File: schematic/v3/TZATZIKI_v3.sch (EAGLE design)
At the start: 7 parts, among them J1 2X20-CHIP-HEADERS2X20CHIP_OFF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, J2 USD-SDIO-SOCKET, J3 USD-SDIO-SOCKET, J4 USD-SDIO-SOCKET, J5 USD-SDIO-SOCKET

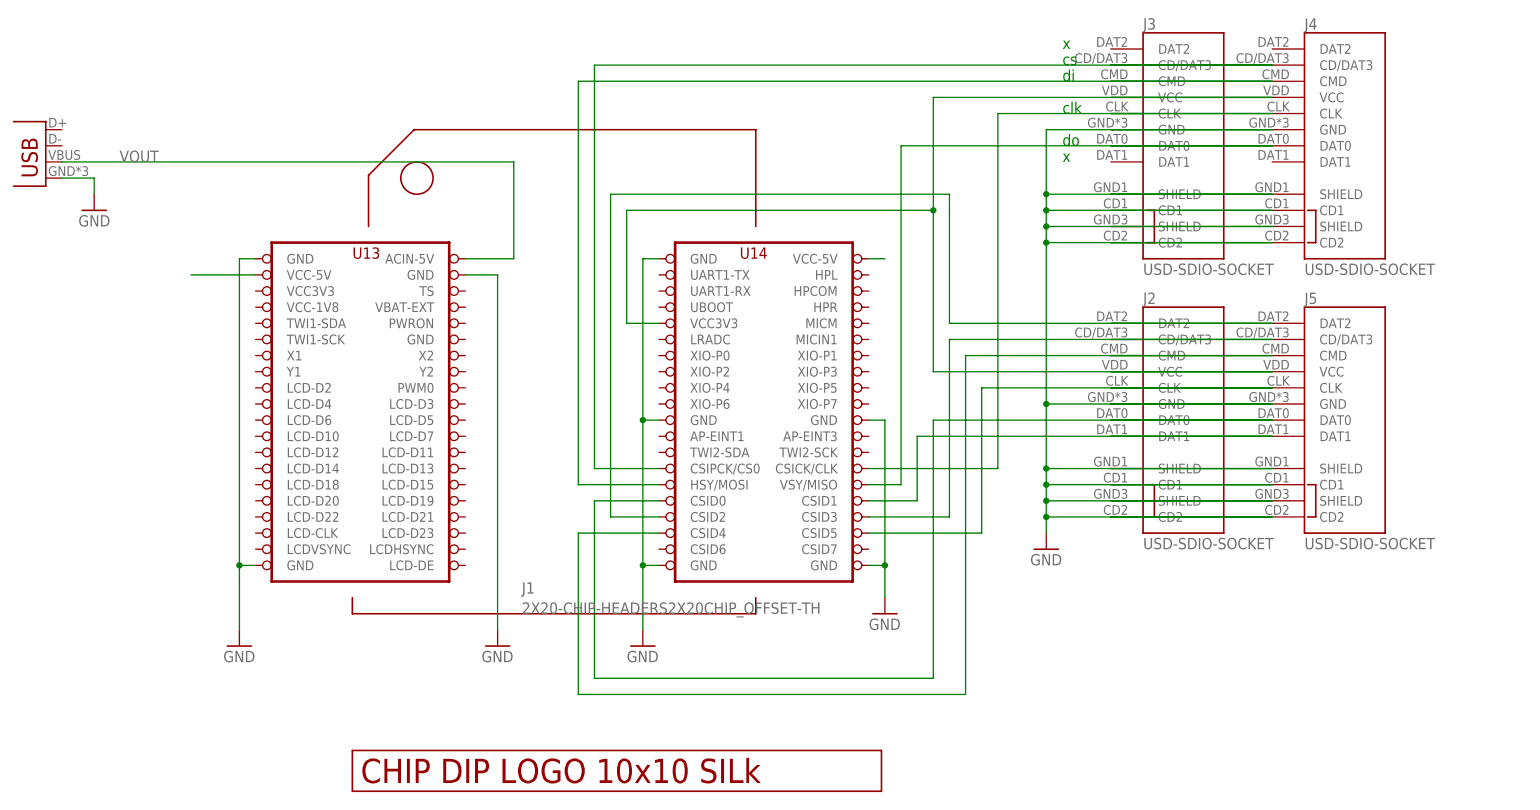
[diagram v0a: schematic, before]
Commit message: added v4 with card detect pin
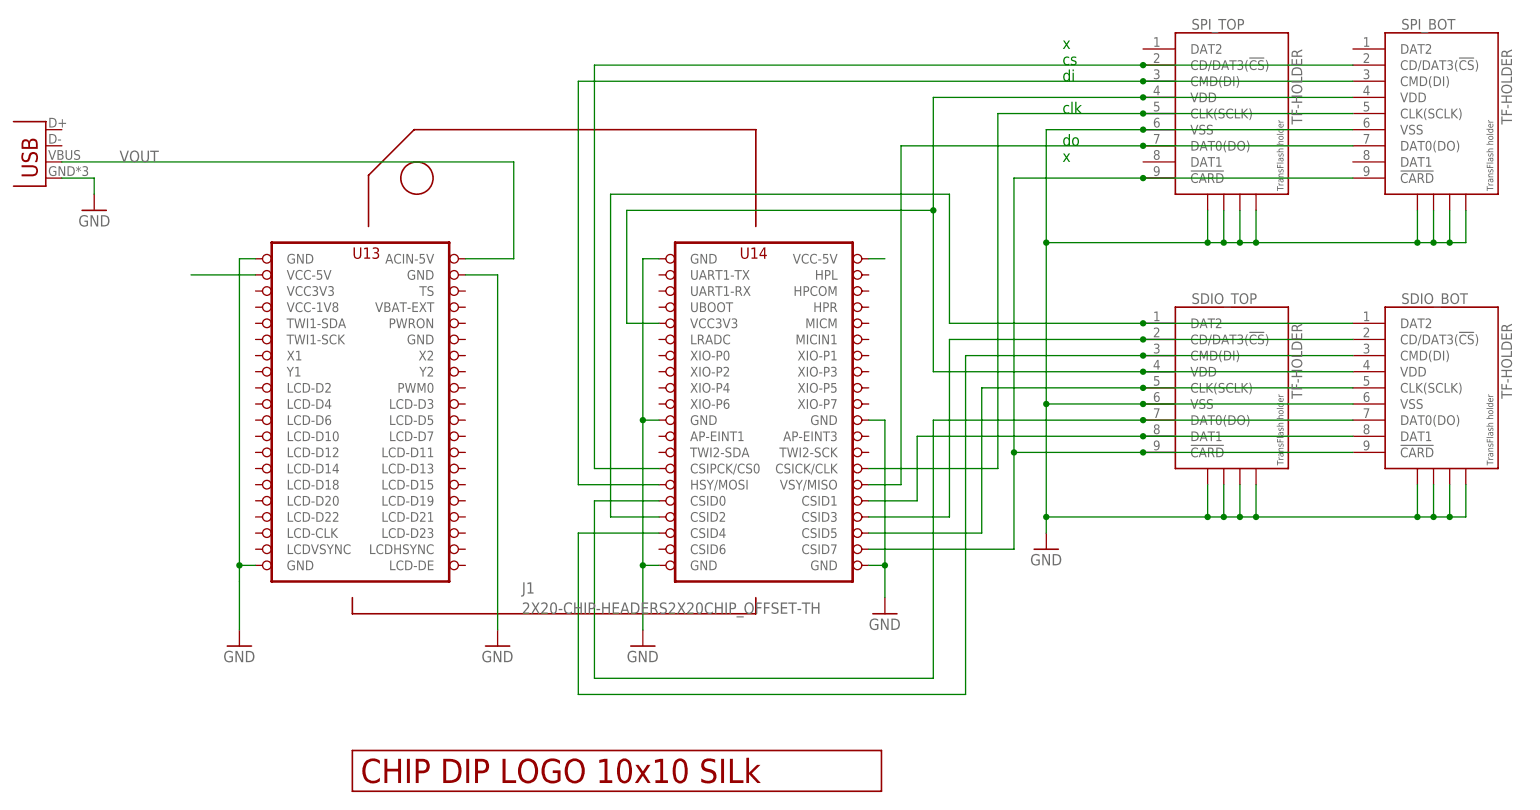
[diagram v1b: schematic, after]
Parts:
- removed J2, J3, J4, J5: USD-SDIO-SOCKET, JKW_CHIP:USD-SDIO-SOCKET
- added SDIO_BOT, SDIO_TOP, SPI_BOT, SPI_TOP: TF-HOLDER, JKW_CHIP:TF-HOLDER
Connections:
- new net N$16: J1.CSID7, SDIO_BOT.!CARD, SDIO_TOP.!CARD, SPI_BOT.!CARD, SPI_TOP.!CARD
- net GND: now also SDIO_BOT.S1, SDIO_BOT.S2, SDIO_BOT.S3, SDIO_BOT.S4, SDIO_BOT.VSS, SDIO_TOP.S1, SDIO_TOP.S2, SDIO_TOP.S3, SDIO_TOP.S4, SDIO_TOP.VSS, SPI_BOT.S1, SPI_BOT.S2, SPI_BOT.S3, SPI_BOT.S4, SPI_BOT.VSS, SPI_TOP.S1, SPI_TOP.S2, SPI_TOP.S3, SPI_TOP.S4, SPI_TOP.VSS; no longer J2.CD1, J2.CD2, J2.GND, J2.SHIELD@1, J2.SHIELD@3, J3.CD1, J3.CD2, J3.GND, J3.SHIELD@1, J3.SHIELD@3, J4.CD1, J4.CD2, J4.GND, J4.SHIELD@1, J4.SHIELD@3, J5.CD1, J5.CD2, J5.GND, J5.SHIELD@1, J5.SHIELD@3
- net N$10: now also SDIO_BOT.VDD, SDIO_TOP.VDD, SPI_BOT.VDD, SPI_TOP.VDD; no longer J2.VCC, J3.VCC, J4.VCC, J5.VCC
- net N$11: now also SPI_BOT.CD/DAT3(!CS!), SPI_TOP.CD/DAT3(!CS!); no longer J3.CD/DAT3, J4.CD/DAT3
- net N$12: now also SPI_BOT.CMD(DI), SPI_TOP.CMD(DI); no longer J3.CMD, J4.CMD
- net N$13: now also SPI_BOT.DAT0(DO), SPI_TOP.DAT0(DO); no longer J3.DAT0, J4.DAT0
- net N$14: now also SPI_BOT.CLK(SCLK), SPI_TOP.CLK(SCLK); no longer J3.CLK, J4.CLK
- net N$2: now also SDIO_BOT.CD/DAT3(!CS!), SDIO_TOP.CD/DAT3(!CS!); no longer J2.CD/DAT3, J5.CD/DAT3
- net N$3: now also SDIO_BOT.DAT0(DO), SDIO_TOP.DAT0(DO); no longer J2.DAT0, J5.DAT0
- net N$4: now also SDIO_BOT.CMD(DI), SDIO_TOP.CMD(DI); no longer J2.CMD, J5.CMD
- net N$5: now also SDIO_BOT.CLK(SCLK), SDIO_TOP.CLK(SCLK); no longer J2.CLK, J5.CLK
- net N$6: now also SDIO_BOT.DAT1, SDIO_TOP.DAT1; no longer J2.DAT1, J5.DAT1
- net N$9: now also SDIO_BOT.DAT2, SDIO_TOP.DAT2; no longer J2.DAT2, J5.DAT2
